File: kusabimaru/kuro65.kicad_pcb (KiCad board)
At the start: 2 copper layers, 174 parts, among them IC1 ATMEGA32U4, J1 ISP, J2 USB4085-GF-A, SW1 SW_Push, Y1 16MHz

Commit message: Added credits and acknowledgements
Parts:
- added REF**: Stabilizer_Cherry_MX_6.25u, Mounting_Keyboard_Stabilizer:Stabilizer_Cherry_MX_6.25u, F.Cu at (173.4, 130.2)
- moved IC1 4.76 mm to (142.5, 130.2)
- turned REF** to 180 degrees

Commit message: Initial component placement done
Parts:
- removed D28, D38: 1N4148, Diode_SMD:D_0805_2012Metric_Pad1.15x1.40mm_HandSolder
- added C9: 100n, Capacitor_SMD:C_0805_2012Metric_Pad1.18x1.45mm_HandSolder, B.Cu at (152.0, 125.4)
- C1, C2, C3, C4, C5, C6, C7, C8, D1, D10, D11, D12, D13, D14, D15, D16, D17, D18, D19, D2, D20, D21, D22, D23, D24, D25, D26, D27, D29, D3, D30, D31, D32, D33, D34, D35, D36, D37, D39, D4, D40, D41, D42, D43, D44, D45, D46, D47, D48, D49, D5, D50, D51, D52, D53, D54, D55, D56, D57, D58, D59, D6, D60, D61, D62, D63, D64, D65, D66, D67, D68, D69, D7, D70, D71, D72, D73, D8, D9, JP1, R1, R2, R3, R4, R5, R6, SW1, Y1: moved to B.Cu
- moved D73 228.9 mm to (337.8, 135.0)
- moved D10 222.9 mm to (78.2, 135.0)
- moved D68 221.4 mm to (318.7, 135.0)
- moved D71 215.2 mm to (337.8, 96.9)
- moved D72 213.9 mm to (337.8, 115.9)
- moved D67 212.3 mm to (318.7, 115.9)
- moved D9 211.6 mm to (75.8, 115.9)
- moved D70 202.9 mm to (337.8, 77.8)
- moved D14 194.2 mm to (94.9, 115.9)
- moved D7 194.1 mm to (80.6, 77.8)
- moved D63 193.0 mm to (299.6, 135.0)
- moved D69 191.9 mm to (337.8, 58.8)
- moved D64 190.1 mm to (327.2, 63.5)
- moved D15 188.3 mm to (102.0, 135.0)
- moved D8 187.6 mm to (85.3, 96.9)
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
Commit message: Some routing done + References added
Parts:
- added C10: 100n, Capacitor_SMD:C_0805_2012Metric_Pad1.18x1.45mm_HandSolder, B.Cu at (152.0, 138.1)
- added C11: 4u7, Capacitor_SMD:C_0805_2012Metric_Pad1.18x1.45mm_HandSolder, B.Cu at (148.5, 121.1)
- C8: footprint Diode_SMD:D_0805_2012Metric_Pad1.15x1.40mm_HandSolder -> Capacitor_SMD:C_0805_2012Metric_Pad1.18x1.45mm_HandSolder
- J1: footprint Connector_PinHeader_1.27mm:PinHeader_2x03_P1.27mm_Vertical -> Connector_PinHeader_2.54mm:PinHeader_2x03_P2.54mm_Vertical
- SW1: value SW_Push -> SW_RESET
- Y1: footprint Crystal:Crystal_SMD_3225-4Pin_3.2x2.5mm_HandSoldering -> Crystal:Crystal_SMD_SeikoEpson_TSX3225-4Pin_3.2x2.5mm_HandSoldering
- moved R5 236.2 mm to (74.7, 84.5), turned to 270 degrees
- moved SW1 235.0 mm to (71.7, 92.3), turned to 270 degrees
- moved C6 33.6 mm to (129.7, 121.9), turned to 90 degrees
- moved J1 32.6 mm to (126.9, 127.3), turned to 270 degrees
- moved JP1 30.6 mm to (157.3, 127.7), turned to 0 degrees
- moved C7 27.5 mm to (136.5, 121.9), turned to 270 degrees
- moved Y1 25.9 mm to (133.1, 122.1)
- moved R6 22.5 mm to (153.3, 127.7), turned to 180 degrees
- moved C4 18.1 mm to (131.7, 134.9), turned to 180 degrees
- moved C8 16.9 mm to (135.5, 136.1)
- moved C3 15.9 mm to (147.9, 138.1), turned to 0 degrees
- moved D51 13.5 mm to (252.9, 124.3), turned to 0 degrees
- moved D6 10.2 mm to (82.2, 57.6)
- moved R3 10.0 mm to (60.5, 62.5)
- moved D3 9.37 mm to (64.6, 98.9), turned to 0 degrees
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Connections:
- net Net-(J2-PadA6) renamed /DCON+
- net Net-(J2-PadA7) renamed /DCON-
- C6 pad 1: Net-(C6-Pad1) -> /XTAL+
- C7 pad 1: Net-(C7-Pad1) -> /XTAL-
- IC1 pad 16: Net-(C6-Pad1) -> /XTAL+
- IC1 pad 17: Net-(C7-Pad1) -> /XTAL-
- SW1 pad 2: RESET -> GND
- SW1 pad 3: (no net) -> RESET
- SW1 pad 4: (no net) -> RESET
- Y1 pad 1: Net-(C6-Pad1) -> /XTAL-
- Y1 pad 2: Net-(C7-Pad1) -> GND
- Y1 pad 3: (no net) -> /XTAL+
- Y1 pad 4: (no net) -> GND
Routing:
- net Row3: track 0.00 -> 426.0 mm, vias 0 -> 2
- net Row1: track 0.00 -> 397.1 mm, vias 0 -> 2
- net Row4: track 0.00 -> 367.7 mm, vias 0 -> 2
- net Row2: track 0.00 -> 357.8 mm, vias 0 -> 2
- net Row5: track 0.00 -> 287.7 mm, vias 0 -> 1
- net VCC: track 0.00 -> 227.2 mm, vias 0 -> 2
- net D-: track 0.00 -> 136.5 mm
- net Col1: track 0.00 -> 136.4 mm, vias 0 -> 4
- net D+: track 0.00 -> 134.1 mm
- net Col15: track 0.00 -> 116.8 mm, vias 0 -> 12
- net Col12: track 0.00 -> 109.8 mm, vias 0 -> 8
- net Col3: track 0.00 -> 109.0 mm, vias 0 -> 7
- net Col13: track 0.00 -> 104.6 mm, vias 0 -> 8
- net Col7: track 0.00 -> 101.8 mm, vias 0 -> 6
- net Col2: track 0.00 -> 99.3 mm, vias 0 -> 8
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- added copper zone on B.Cu, net GND
- added copper zone on F.Cu, net GND
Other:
- net class Default: trace_width 0.25 -> 0.4
- net class Power added: clearance 0.2, trace_width 0.8, via_dia 0.8, via_drill 0.4
- net class USB added: clearance 0.15, trace_width 0.4, via_dia 0.8, via_drill 0.4
- net class XTAL added: clearance 0.25, trace_width 0.4, via_dia 0.8, via_drill 0.4
- rule trace_min: 0.2 -> 0.127
- rule via_min_size: 0.4 -> 0.6

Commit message: Routing completed. Some modifications still needed.
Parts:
- moved J1 6.18 mm to (132.6, 129.7)
- moved D33 1.29 mm to (173.4, 133.7)
- moved C10 1.10 mm to (153.1, 138.1)
- moved C4 1.08 mm to (130.7, 135.3)
- moved JP1 0.92 mm to (156.7, 128.4), turned to 270 degrees
- moved C8 0.85 mm to (134.7, 136.4)
- moved D51 0.67 mm to (252.6, 124.9)
- moved R6 0.20 mm to (153.5, 127.7)
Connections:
- IC1 pad 12: Col16 -> Col2
- IC1 pad 18: Col2 -> Col3
- IC1 pad 19: Col3 -> Col4
- IC1 pad 20: Col4 -> Col5
- IC1 pad 21: Col5 -> Col6
- IC1 pad 25: Col6 -> Col8
- IC1 pad 26: Col8 -> Col9
- IC1 pad 27: Col9 -> Col10
- IC1 pad 28: Col13 -> Col11
- IC1 pad 29: Col14 -> Col12
- IC1 pad 30: Col15 -> Col13
- IC1 pad 31: Col10 -> Col14
- IC1 pad 32: Col11 -> Col15
- IC1 pad 36: Col1 -> Col16
- IC1 pad 37: Row5 -> Row1
- IC1 pad 38: Row4 -> Row2
- IC1 pad 40: Row2 -> Row4
- IC1 pad 41: Row1 -> Row5
- IC1 pad 8: Col12 -> Col1
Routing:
- net Col16: track 91.3 -> 295.5 mm, vias 8 -> 10
- net Col15: track 116.8 -> 306.1 mm, vias 12 -> 16
- net Col14: track 81.7 -> 262.0 mm, vias 8 -> 12
- net Col13: track 104.6 -> 264.1 mm, vias 8 -> 10
- net Row1: track 397.1 -> 534.2 mm, vias 2 -> 10
- net Col12: track 109.8 -> 233.2 mm, vias 8 -> 10
- net Row2: track 357.8 -> 473.6 mm, vias 2 -> 6
- net Row3: track 426.0 -> 540.5 mm, vias 2 -> 4
- net Col11: track 86.1 -> 195.4 mm, vias 8 -> 10
- net Col1: track 136.4 -> 225.0 mm, vias 4 -> 6
- net Col10: track 77.3 -> 165.7 mm, vias 6 -> 8
- net Row4: track 367.7 -> 450.9 mm, vias 2 -> 4
- net Row5: track 287.7 -> 368.7 mm, vias 1 -> 3
- net Col9: track 77.2 -> 147.2 mm, vias 6 -> 8
- net RESET: track 28.0 -> 97.4 mm, vias 0 -> 2
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
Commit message: Added logo to project and placed on PCB.
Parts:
- added G***: LOGO, logo:kuro65, F.Cu at (208.8, 127.4)
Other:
- board outline added: 304.8 x 95.3 mm

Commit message: Some PCB adjustments.
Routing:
- net Row5: track 368.7 -> 365.1 mm
- net Net-(D33-Pad1): track 10.6 -> 11.1 mm
- net VCC: track 238.8 -> 239.4 mm
- net GND: vias 7 -> 85

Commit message: Exchanged diode footpint to SOD-323
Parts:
- removed G***: LOGO, logo:kuro65
- D1, D10, D11, D12, D13, D14, D15, D16, D17, D18, D19, D2, D20, D21, D22, D23, D24, D25, D26, D27, D29, D3, D30, D31, D32, D33, D34, D35, D36, D37, D39, D4, D40, D41, D42, D43, D44, D45, D46, D47, D48, D49, D5, D50, D51, D52, D53, D54, D55, D56, D57, D58, D59, D6, D60, D61, D62, D63, D64, D65, D66, D67, D68, D69, D7, D70, D71, D72, D73, D8, D9: footprint Diode_SMD:D_0805_2012Metric_Pad1.15x1.40mm_HandSolder -> Diode_SMD:D_SOD-323_HandSoldering
- moved R1 1.17 mm to (51.5, 46.5)
- moved R2 1.08 mm to (70.6, 46.5)
- moved D6 0.30 mm to (82.2, 57.9)
- moved D61 0.20 mm to (285.0, 134.9)
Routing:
- net Col16: track 295.9 -> 297.2 mm
- net Col12: track 233.2 -> 232.1 mm
- net Col3: track 149.1 -> 148.1 mm
- net Net-(J2-PadA5): track 13.8 -> 12.8 mm
- net Col11: track 195.5 -> 194.5 mm
- net Col4: track 103.0 -> 102.1 mm
- net Col6: track 97.9 -> 97.0 mm
- net Col2: track 154.7 -> 153.9 mm
- net Col7: track 135.3 -> 134.5 mm
- net Col10: track 165.8 -> 165.0 mm
- net Col5: track 86.1 -> 85.4 mm

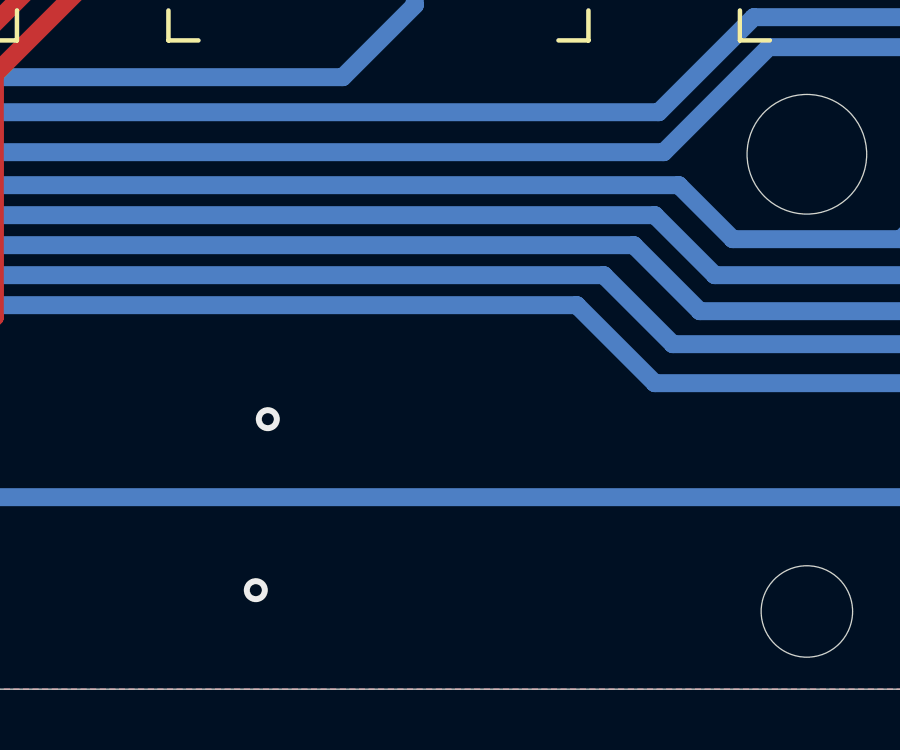
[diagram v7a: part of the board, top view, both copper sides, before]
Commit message: Added additional logos and some 3D render pictures
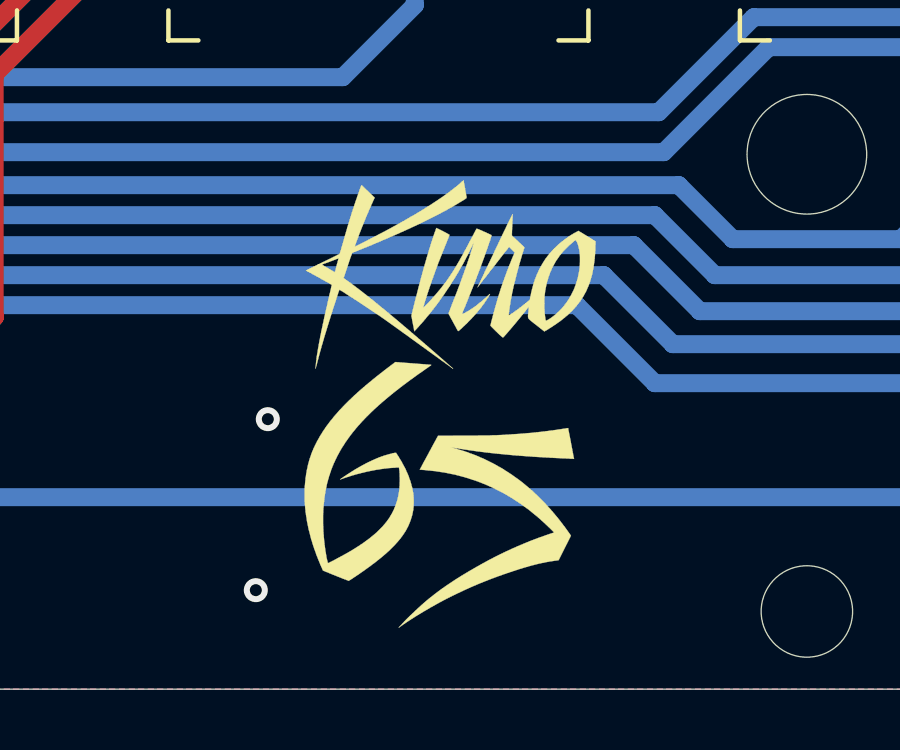
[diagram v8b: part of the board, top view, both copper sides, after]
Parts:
- added G***: LOGO, logo:kuro65stilltime, F.Cu at (211.5, 130.3)
